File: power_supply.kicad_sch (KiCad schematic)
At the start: 7 parts, among them J1 USB_C_Receptacle_USB2.0_16P, U1 AP2112K-3.3

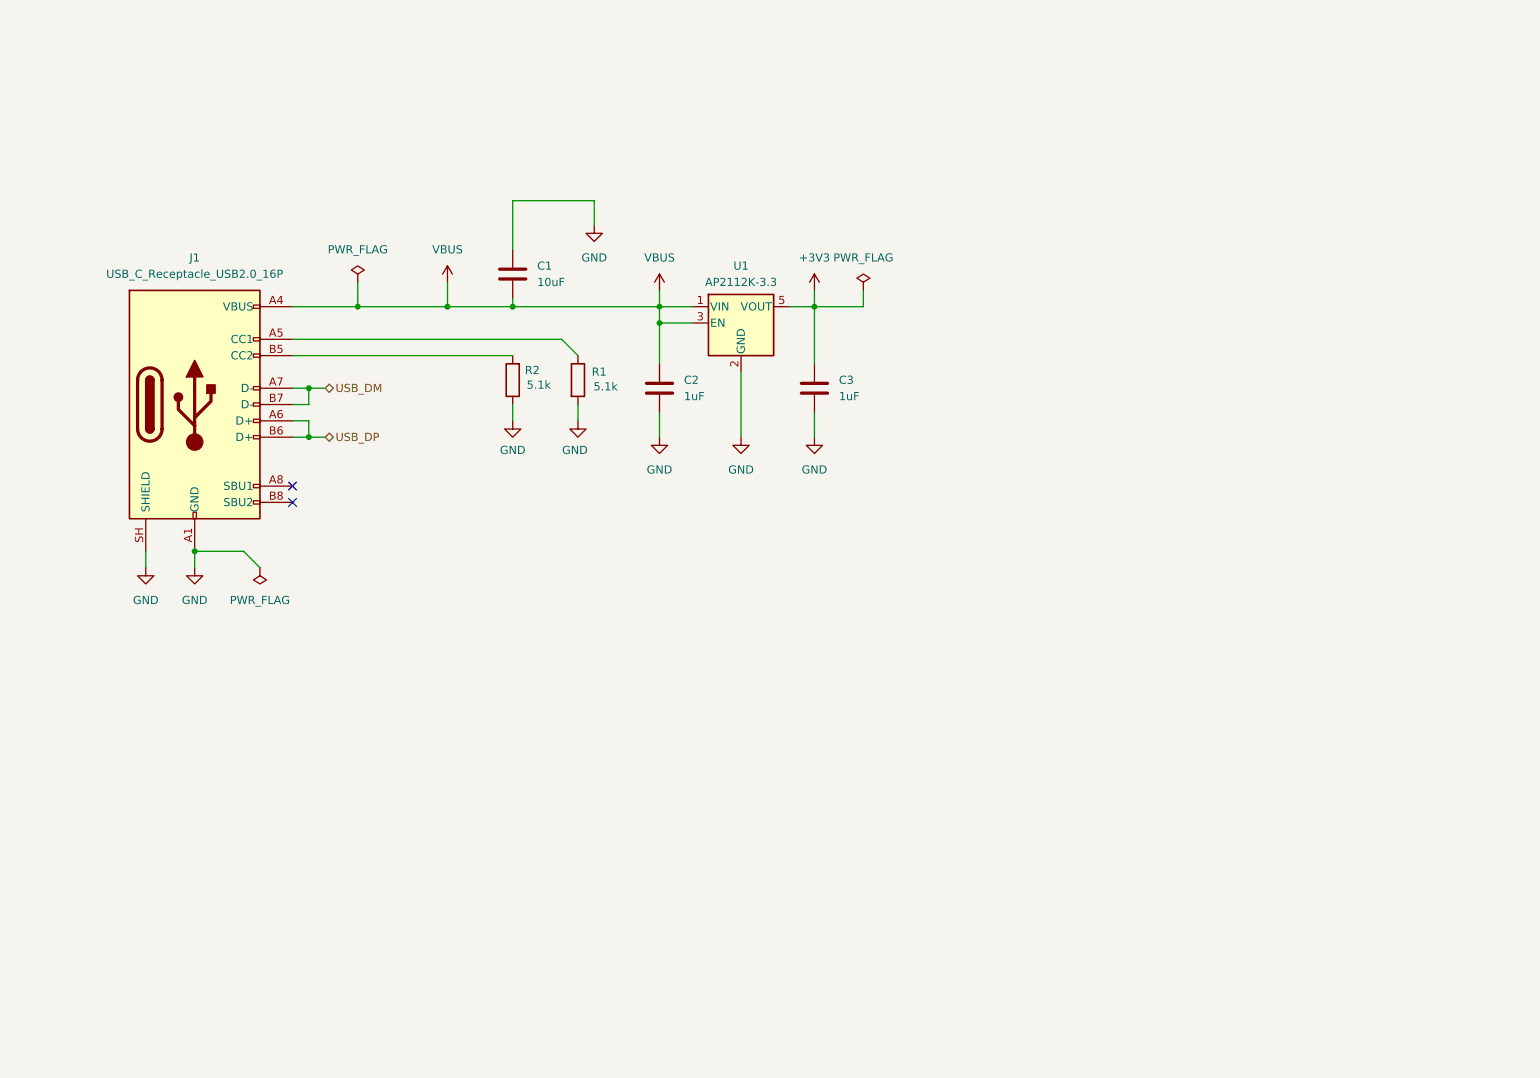
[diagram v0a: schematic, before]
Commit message: Add dual-LDO selector, power LEDs, current measurement jumper
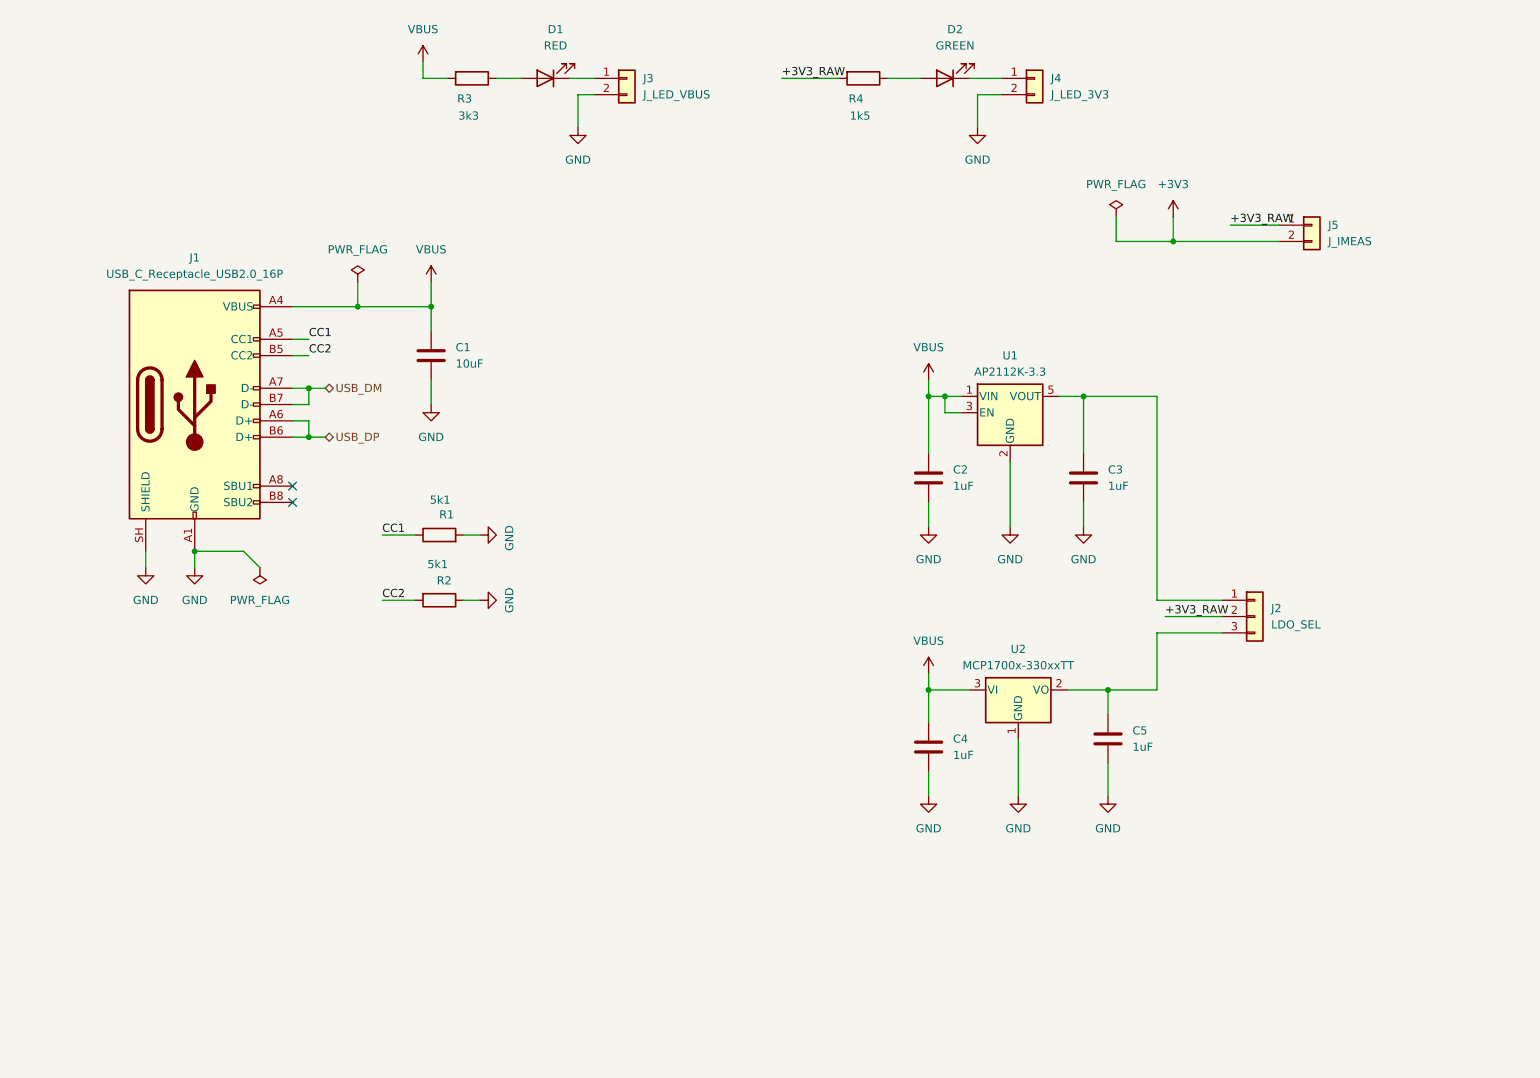
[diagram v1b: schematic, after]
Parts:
- added C4, C5: 1uF, symbol Device:C
- added D1: RED, LED_SMD:LED_0603_1608Metric_Pad1.05x0.95mm_HandSolder, symbol Device:LED
- added D2: GREEN, LED_SMD:LED_0603_1608Metric_Pad1.05x0.95mm_HandSolder, symbol Device:LED
- added J2: LDO_SEL, Connector_PinHeader_2.54mm:PinHeader_1x03_P2.54mm_Vertical, symbol Connector_Generic:Conn_01x03
- added J3: J_LED_VBUS, Connector_PinHeader_2.54mm:PinHeader_1x02_P2.54mm_Vertical, symbol Connector_Generic:Conn_01x02
- added J4: J_LED_3V3, Connector_PinHeader_2.54mm:PinHeader_1x02_P2.54mm_Vertical, symbol Connector_Generic:Conn_01x02
- added J5: J_IMEAS, Connector_PinHeader_2.54mm:PinHeader_1x02_P2.54mm_Vertical, symbol Connector_Generic:Conn_01x02
- added R3: 3k3, Resistor_SMD:R_0603_1608Metric_Pad0.98x0.95mm_HandSolder, symbol Device:R
- added R4: 1k5, Resistor_SMD:R_0603_1608Metric_Pad0.98x0.95mm_HandSolder, symbol Device:R
- added U2: MCP1700x-330xxTT, Package_TO_SOT_SMD:SOT-23_Handsoldering, symbol Regulator_Linear:MCP1700x-330xxTT
- R1, R2: value 5.1k -> 5k1
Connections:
- net +3V3: now also J5.2 (Pin_2); no longer C3.1, U1.5 (VOUT)
- net GND: now also C1.2, C4.2, C5.2, J3.2 (Pin_2), J4.2 (Pin_2), U2.1 (GND); no longer C1.1
- net VBUS: now also C1.1, C4.1, R3.2, U2.3 (VI); no longer C1.2
- net CC2: now reaches J1.B5 (CC2), R2.2
- net CC1: now reaches J1.A5 (CC1), R1.1
- new net: D1.1 (K), J3.1 (Pin_1)
- new net: D1.2 (A), R3.1
- new net: D2.1 (K), J4.1 (Pin_1)
- new net: C3.1, J2.1 (Pin_1), U1.5 (VOUT)
- new net: C5.1, J2.3 (Pin_3), U2.2 (VO)
- new net: D2.2 (A), R4.1
- new net +3V3_RAW: J2.2 (Pin_2), J5.1 (Pin_1), R4.2
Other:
- moved on the sheet: C1, C2, C3, R1, R2, U1

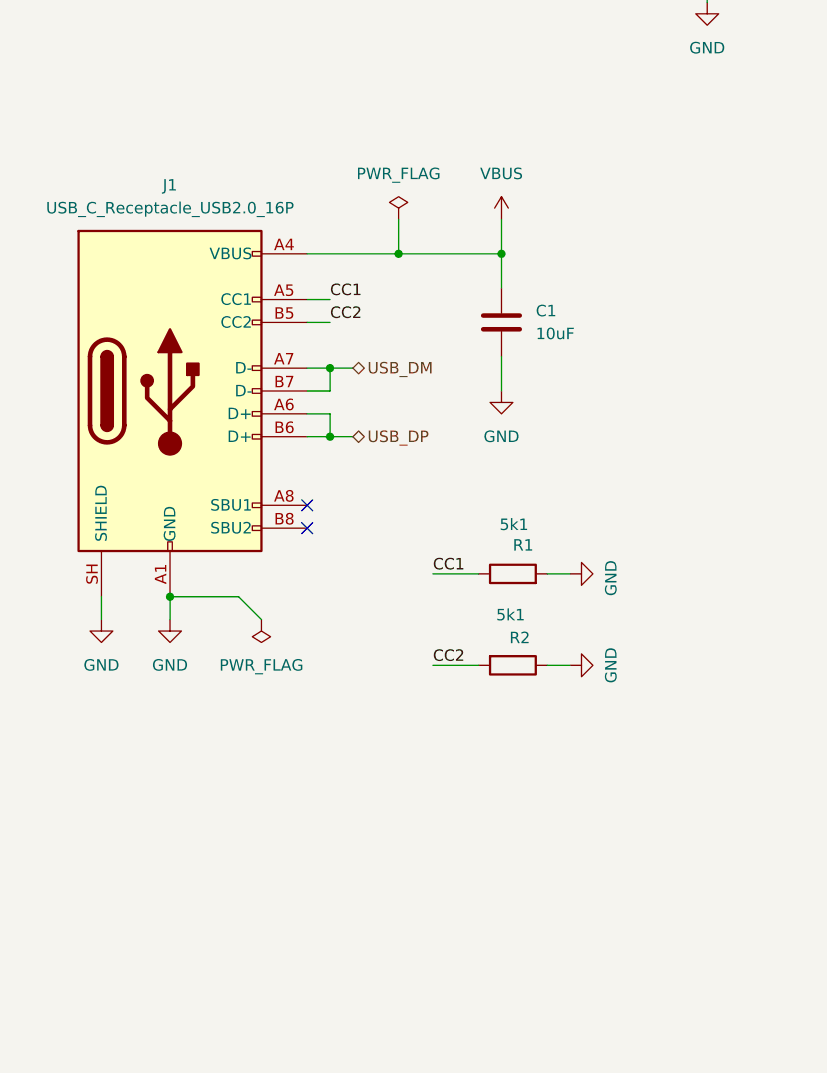
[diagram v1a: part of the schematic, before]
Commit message: Complete MCU power, debug, and boot circuits; add scope doc
Schematic additions:
- Add second Schottky on USB VBUS for full diode-OR protection
- Wire VBAT, VSS, VSSA to power nets
- Add VDD decoupling: 3x 100nF + 1x 4.7uF bulk
- Add VDDA filter: ferrite bead + 1uF + 10nF
- Add VREF+ selector jumper with decoupling and external input
- Wire USB_DP/USB_DM to PA12/PA11 (corrected pinout)
- Add SWD 5-pin header on PA13/PA14/NRST
- Add reset button with 100nF noise cap
- Add BOOT0 button on PB8 with 10k pull-down

Project documentation:
- Add docs/scope.md locking v1 feature list and v2 candidates
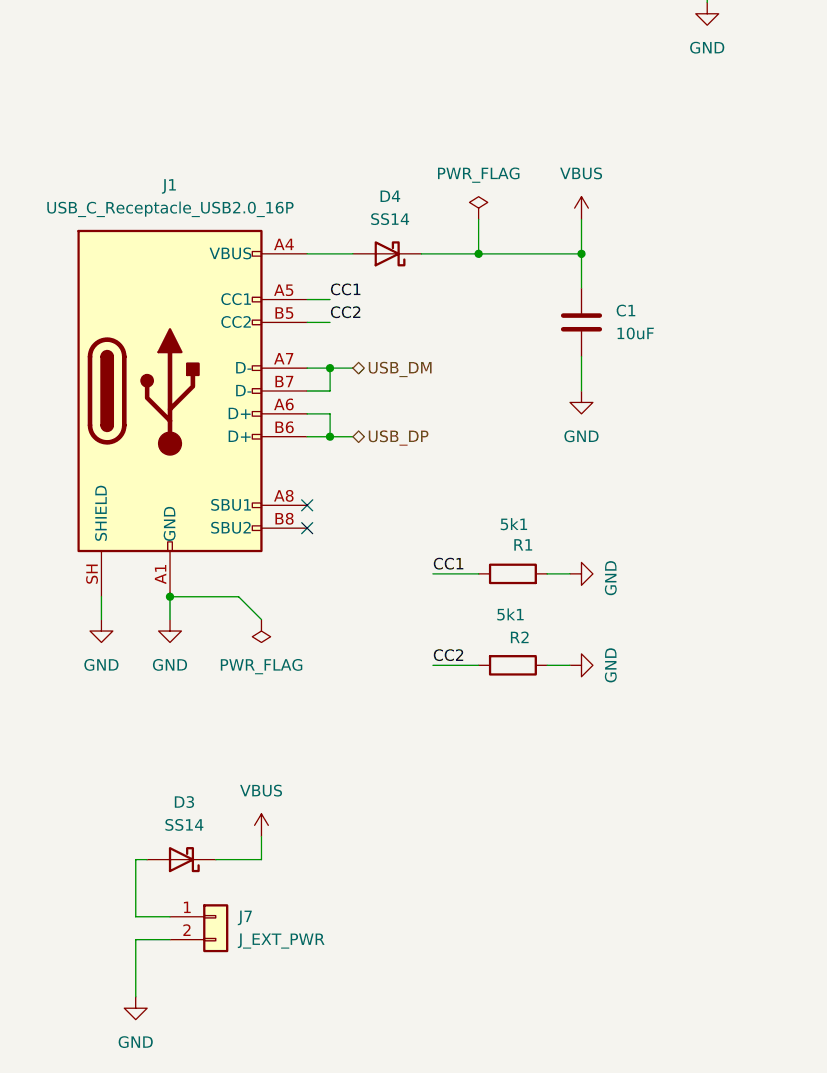
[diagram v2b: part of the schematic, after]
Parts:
- added D3, D4: SS14, Diode_SMD:D_SOD-123, symbol Device:D_Schottky
- added J7: J_EXT_PWR, Connector_JST:JST_PH_S2B-PH-K_1x02_P2.00mm_Horizontal, symbol Connector_Generic:Conn_01x02
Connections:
- net GND: now also J7.2 (Pin_2)
- net VBUS: now also D3.1 (K), D4.1 (K); no longer J1.A4 (VBUS), J1.A9 (VBUS), J1.B4 (VBUS), J1.B9 (VBUS)
- new net: D3.2 (A), J7.1 (Pin_1)
- new net: D4.2 (A), J1.A4 (VBUS), J1.A9 (VBUS), J1.B4 (VBUS), J1.B9 (VBUS)
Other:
- moved on the sheet: C1

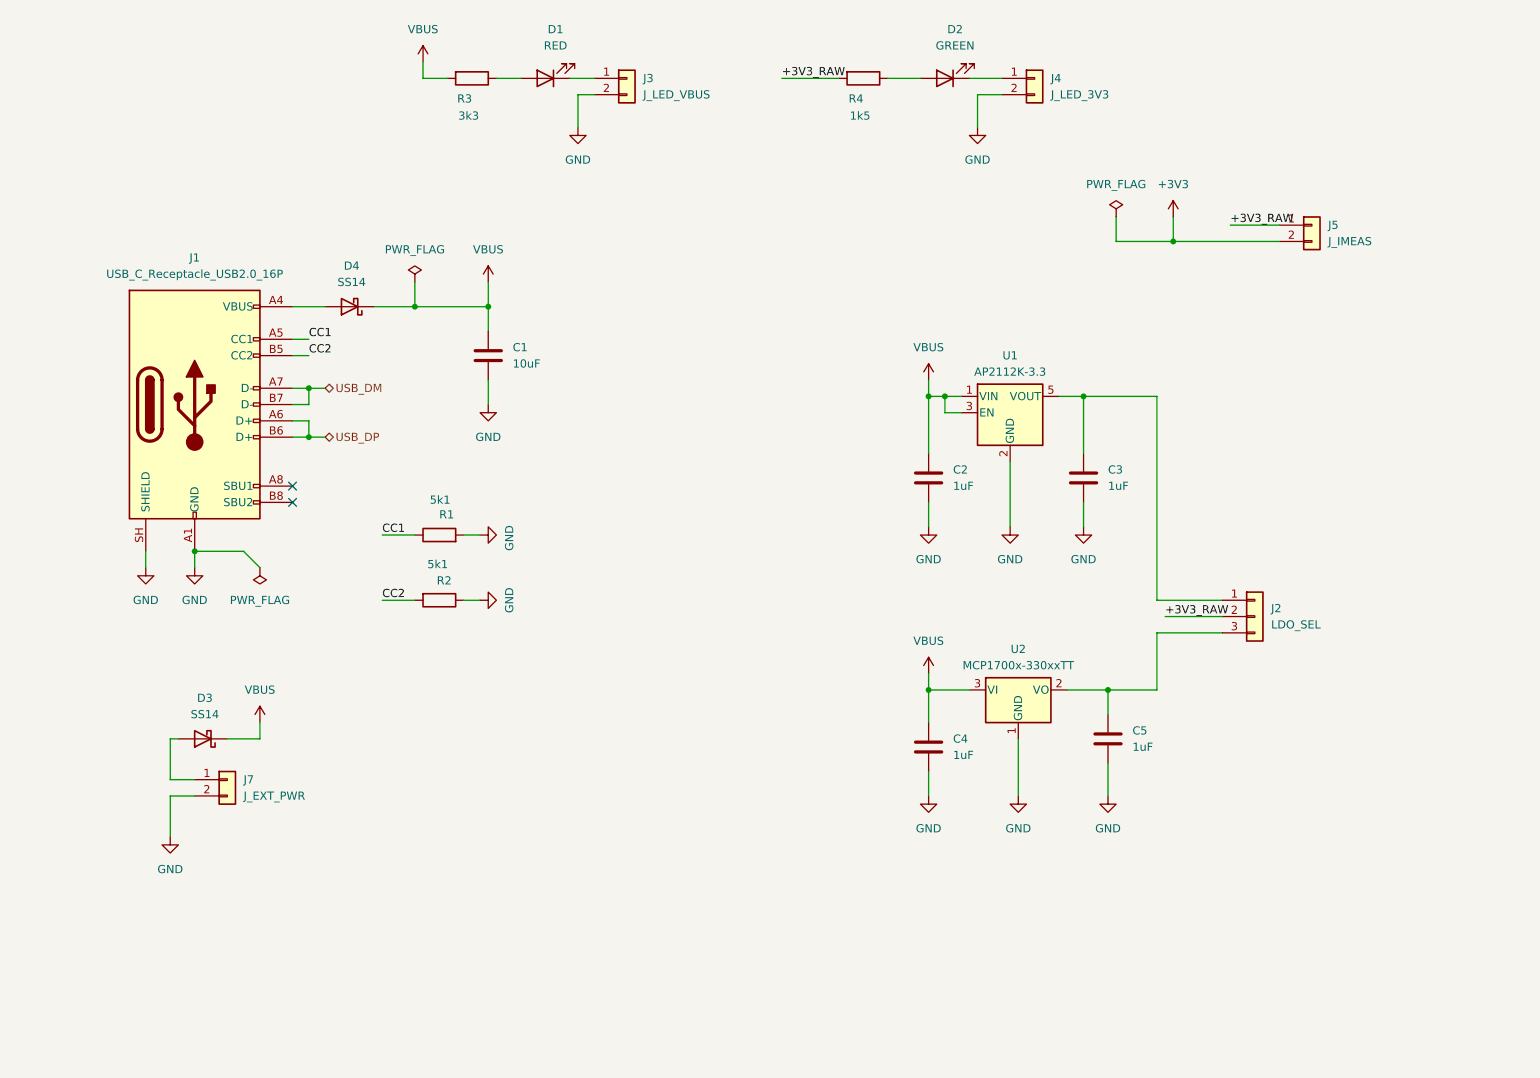
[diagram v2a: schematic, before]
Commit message: feat(schematic): complete v0.1 schematic for STM32G431 dev board
Three-sheet hierarchical design with clean ERC pass (0 errors, 0 warnings).

MCU (mcu.kicad_sch):
- STM32G431CBTx LQFP-48
- VDD decoupling (3× 100nF + 1× 4.7µF)
- VDDA filter via ferrite bead + 1µF + 10nF
- VREF+ selector jumper (internal +3V3A or external via 1kΩ series)
- SWD 5-pin header
- Reset button + 100nF noise cap
- BOOT0 button + 10kΩ pull-down

Power Supply (power_supply.kicad_sch):
- USB-C input (GCT USB4085) with 5.1kΩ CC pull-downs
- Diode-OR (SS14): USB + external JST 2-pin
- Dual LDO selector: AP2112K-3.3 and MCP1700-3302
- Current measurement jumper
- Power LEDs with disable jumpers
- USBLC6-2SC6 ESD protection on USB D+/D- with 100nF decoupling

GPIO Breakout (gpio_breakout.kicad_sch):
- 2× 20-pin headers, Black Pill style (40 pins total)
- Buses for PA, PB, PC, PF signal groups
- User LED on PB9 (470Ω current limit)
- User button on PB7 (10kΩ pull-up + 100nF debounce)
- UART header (USART2 on PA2/PA3) with 1kΩ series protection
- VREF_EXT_IN routed for external ADC reference
- NRST exposed for external reset access

USB and SWD signals routed individually; PA11-14 deliberately excluded
from the PA bus to keep USB/SWD pins isolated from the breakout.

Scope changes from initial plan:
- WS2812B RGB LEDs and 74AHCT125 level shifter moved to a separate
  follow-up board (Addressable RGB Demo)
- User LED moved from PA5 to PB9, user button moved from PB1 to PB7,
  freeing high-value ADC pins on the breakout
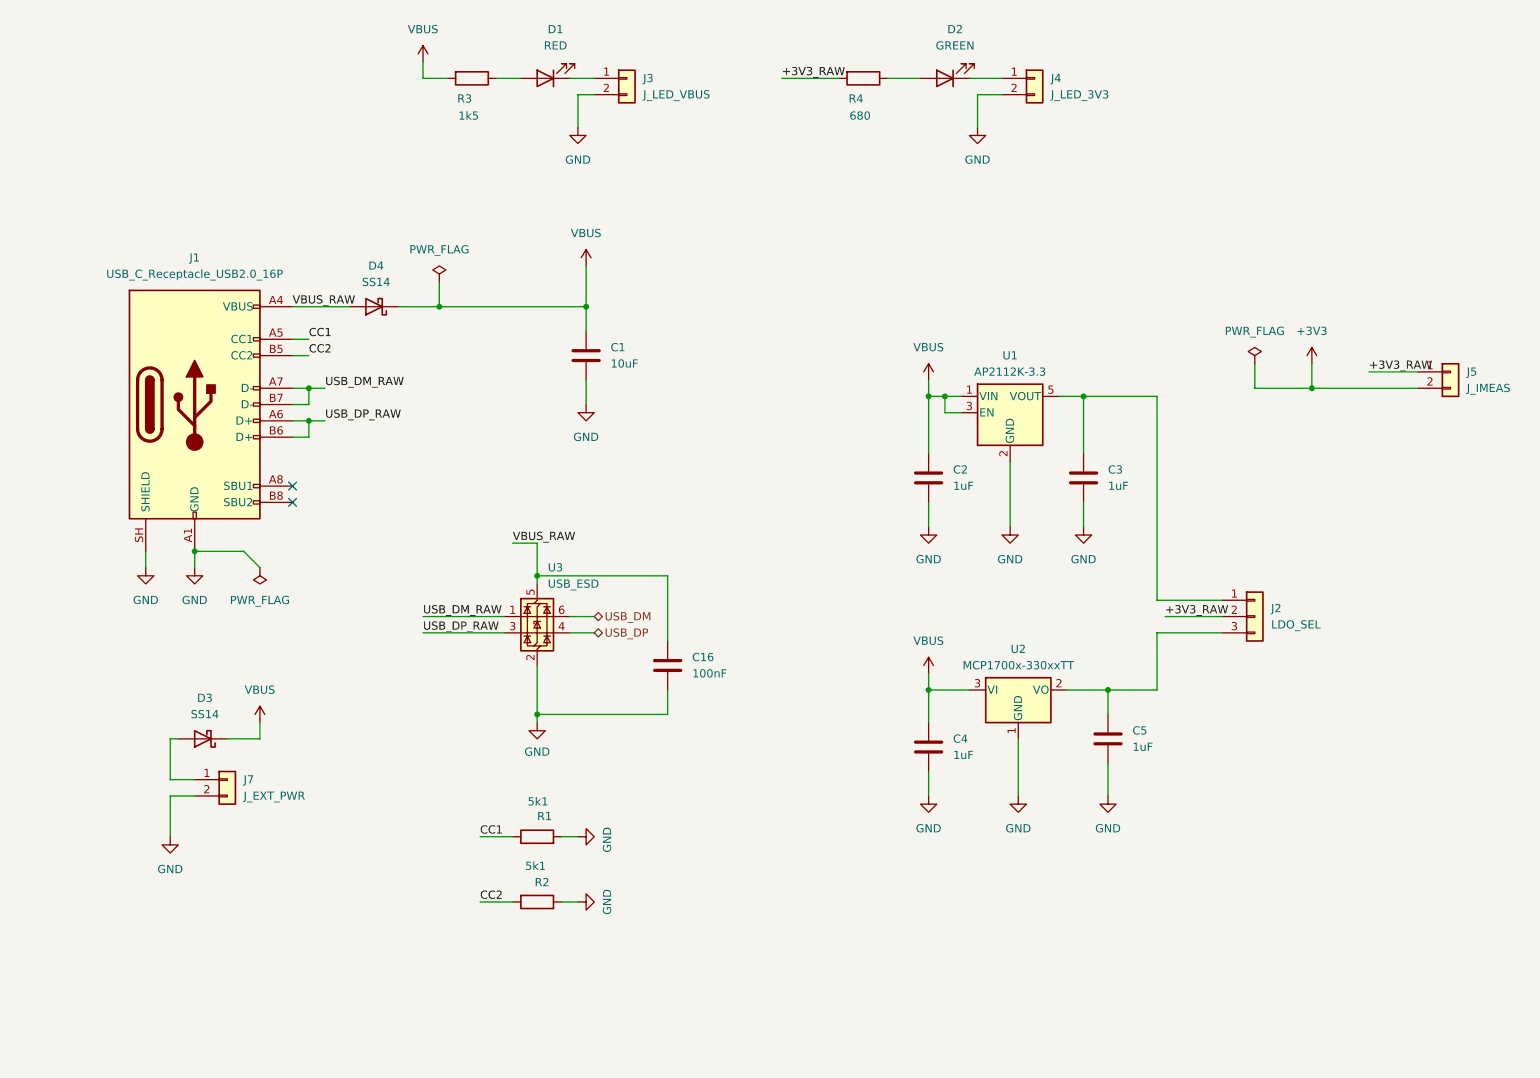
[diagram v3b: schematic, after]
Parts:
- added C16: 100nF, Capacitor_SMD:C_0603_1608Metric_Pad1.08x0.95mm_HandSolder, symbol Device:C
- added U3: USB_ESD, Package_TO_SOT_SMD:SOT-23-6_Handsoldering, symbol Power_Protection:USBLC6-2SC6
- R3: value 3k3 -> 1k5
- R4: value 1k5 -> 680
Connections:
- net GND: now also C16.2, U3.2 (GND)
- net USB_DM: now also U3.6 (I/O1); no longer J1.A7 (D-), J1.B7 (D-)
- net USB_DP: now also U3.4 (I/O2); no longer J1.A6 (D+), J1.B6 (D+)
- net VBUS_RAW: now reaches D4.2 (A), J1.A4 (VBUS), J1.A9 (VBUS), J1.B4 (VBUS), J1.B9 (VBUS)
- net VBUS_RAW: now also C16.1, U3.5 (VBUS)
- new net USB_DM_RAW: J1.A7 (D-), J1.B7 (D-), U3.1 (I/O1)
- new net USB_DP_RAW: J1.A6 (D+), J1.B6 (D+), U3.3 (I/O2)
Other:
- moved on the sheet: C1, D4, J5, R1, R2
